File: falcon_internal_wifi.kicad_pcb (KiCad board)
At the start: 2 copper layers, 25.5 x 34.5 mm, 16 parts, among them J1 Conn_01x05, U1 LM1117-3.3, U2 ESP-12F, U3 NC7ST04M5X

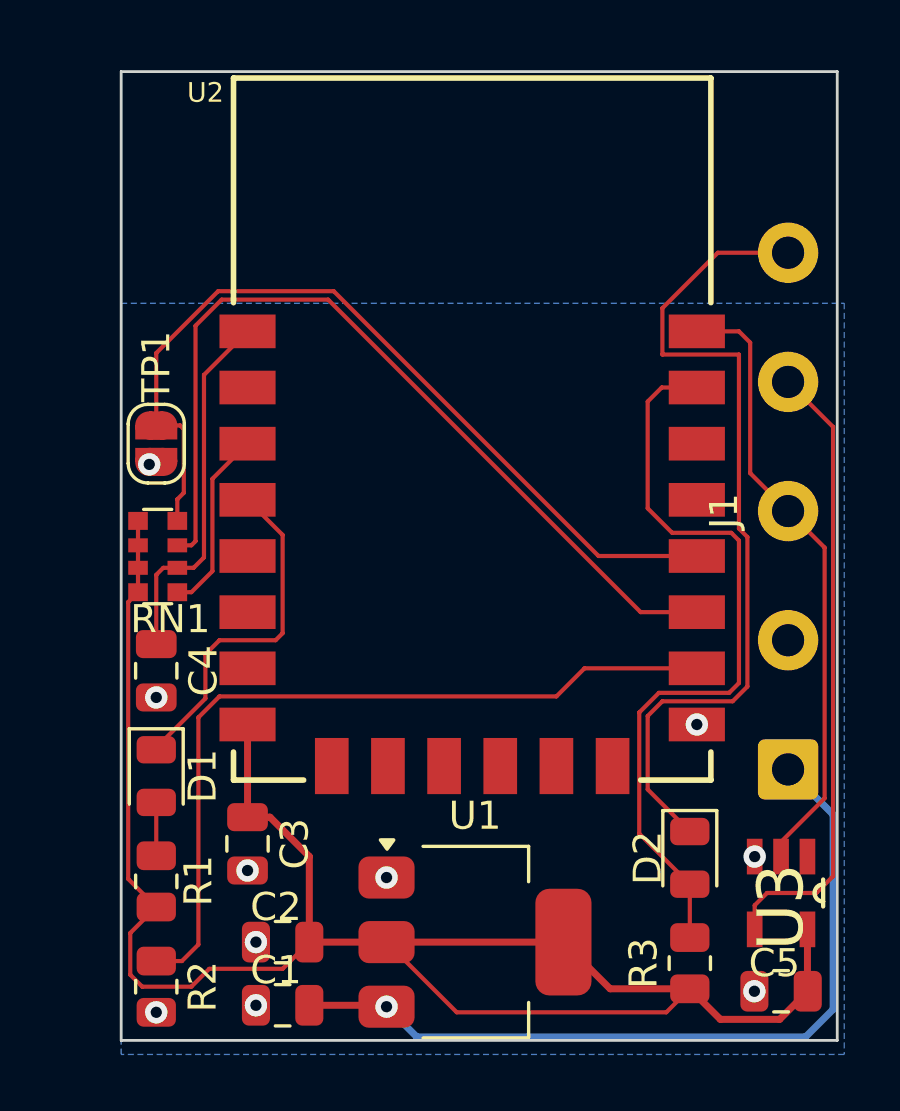
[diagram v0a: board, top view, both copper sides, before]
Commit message: Second design with smaller passive
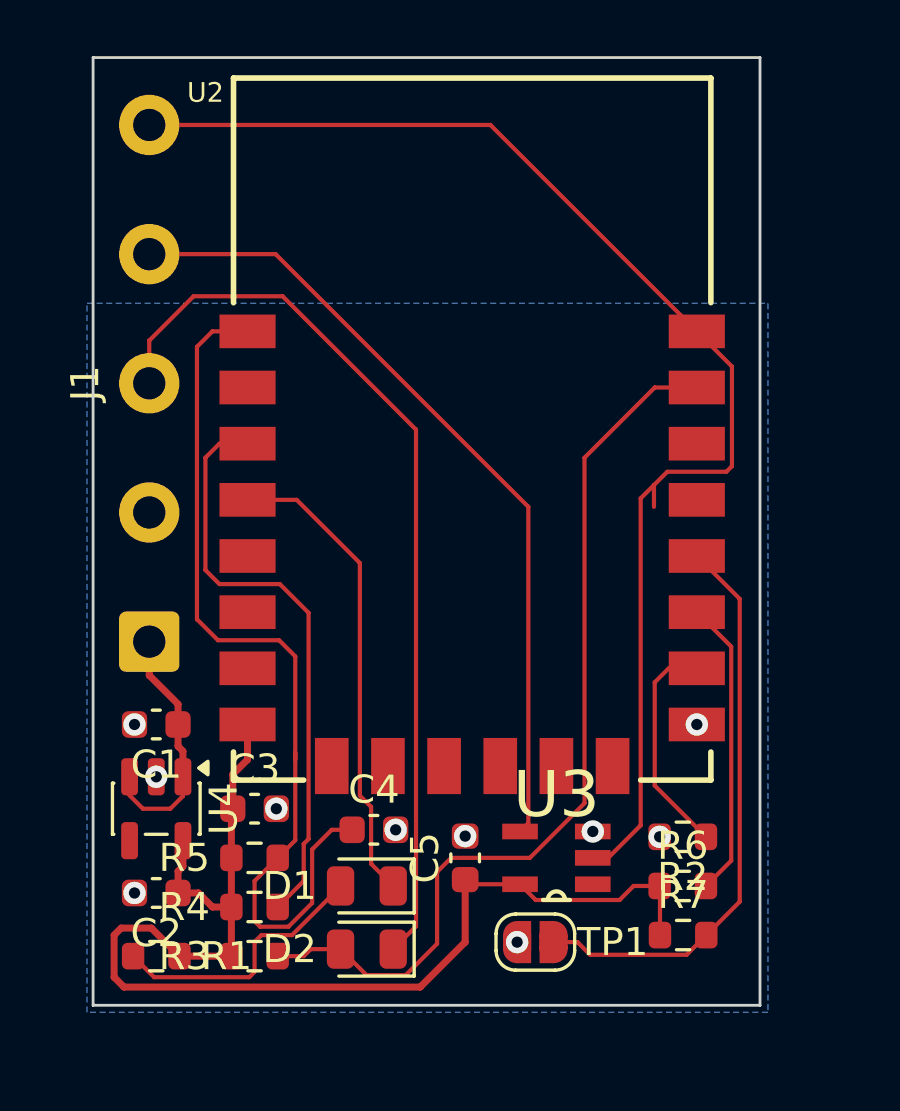
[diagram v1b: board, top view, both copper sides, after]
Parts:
- removed RN1: 10k, Resistor_SMD:R_Array_Convex_4x0612
- removed U1: LM1117-3.3, Package_TO_SOT_SMD:SOT-223-3_TabPin2
- added R4: 1k, Resistor_SMD:R_0603_1608Metric, F.Cu at (102.0, 74.5)
- added R5: 1k, Resistor_SMD:R_0603_1608Metric, F.Cu at (102.0, 72.8)
- added R6: 1k, Resistor_SMD:R_0603_1608Metric, F.Cu at (117.2, 73.8)
- added R7: 1k, Resistor_SMD:R_0603_1608Metric, F.Cu at (117.3, 75.5)
- added U4: TLV73333PDBV, Package_TO_SOT_SMD:SOT-23-5, F.Cu at (98.5, 71.0)
- C1, C2: value 1u -> 100n; footprint Capacitor_SMD:C_0805_2012Metric -> Capacitor_SMD:C_0603_1608Metric
- C3, C4, C5: footprint Capacitor_SMD:C_0805_2012Metric -> Capacitor_SMD:C_0603_1608Metric
- R1, R2, R3: footprint Resistor_SMD:R_0805_2012Metric -> Resistor_SMD:R_0603_1608Metric
- moved J1 23.2 mm to (98.2, 65.1)
- moved TP1 22.3 mm to (112.0, 75.8), turned to 180 degrees
- moved R2 19.5 mm to (117.2, 72.0), turned to 180 degrees
- moved R3 15.5 mm to (102.0, 76.2), turned to 0 degrees
- moved C5 12.2 mm to (109.5, 72.8), turned to 90 degrees
- moved D2 12.0 mm to (106.0, 76.0), turned to 180 degrees
- moved C1 11.0 mm to (98.5, 68.0)
- moved C4 9.60 mm to (106.2, 71.8), turned to 0 degrees
- moved D1 8.46 mm to (106.0, 73.8), turned to 180 degrees
- moved U3 8.10 mm to (112.8, 72.8), turned to 180 degrees
- moved C2 4.83 mm to (98.5, 74.0)
- moved R1 2.66 mm to (98.5, 76.2), turned to 180 degrees
- moved C3 1.27 mm to (102.0, 71.0), turned to 0 degrees
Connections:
- J1 pad 3: /TX -> /RX
- J1 pad 5: /RX -> /TX
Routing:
- net /TX: track 22.1 -> 46.2 mm
- net +3.3V: track 67.1 -> 43.4 mm
- net Net-(U2-GPIO2): track 31.2 -> 10.6 mm
- net Net-(U2-GPIO15): track 28.3 -> 7.96 mm
- net +5V: track 28.8 -> 8.94 mm, vias 1 -> 0
- net Net-(U2-RST): track 13.9 -> 32.2 mm
- net Net-(U2-EN): track 7.12 -> 20.9 mm
- net /FLASH: track 31.0 -> 20.5 mm
- net Net-(D1-A): track 1.90 -> 9.68 mm
- net /~{TX}: track 22.3 -> 28.9 mm
- net Net-(D2-A): track 27.3 -> 32.8 mm
- net /STATUS: track 12.5 -> 16.9 mm
- net /RX: track 30.3 -> 32.5 mm
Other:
- board size 25.5 x 34.5 mm -> 23.8 x 33.8 mm

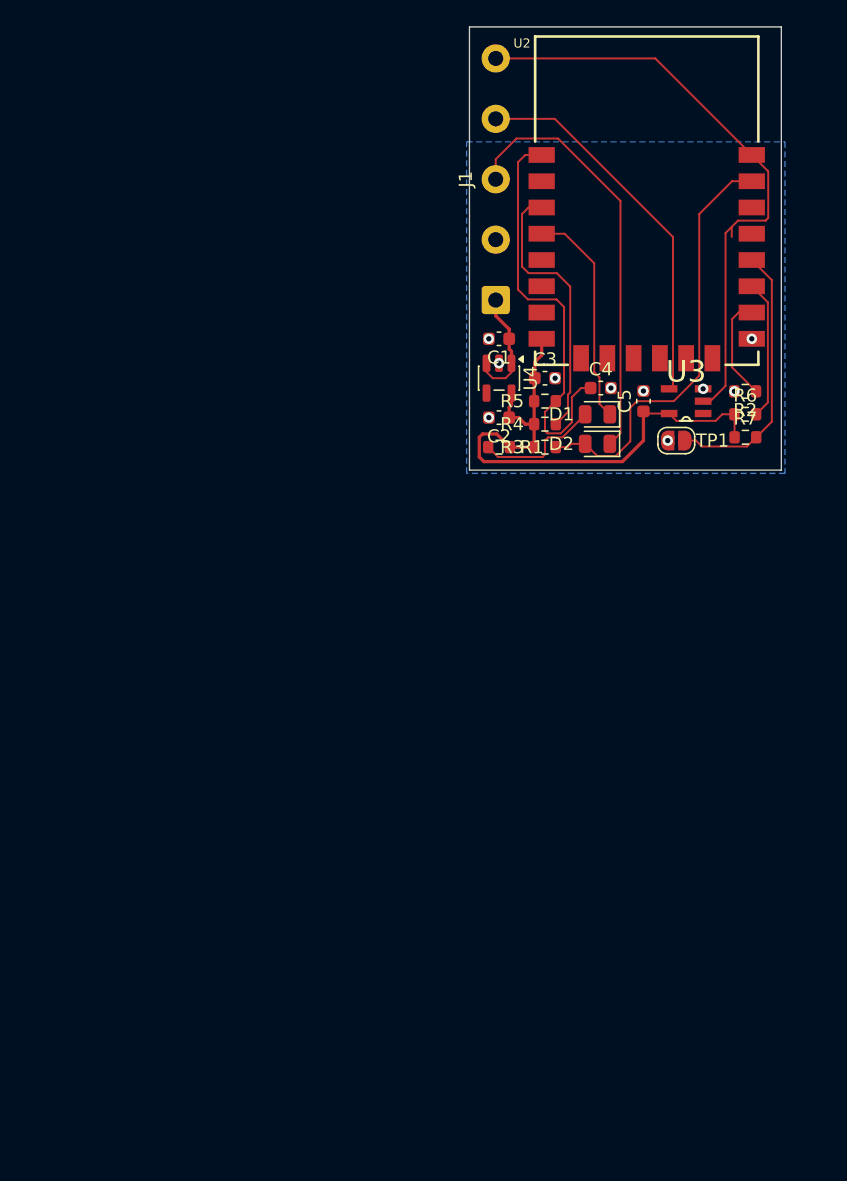
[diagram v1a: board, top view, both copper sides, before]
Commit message: Version as quoted. Considering just going back to 0805.
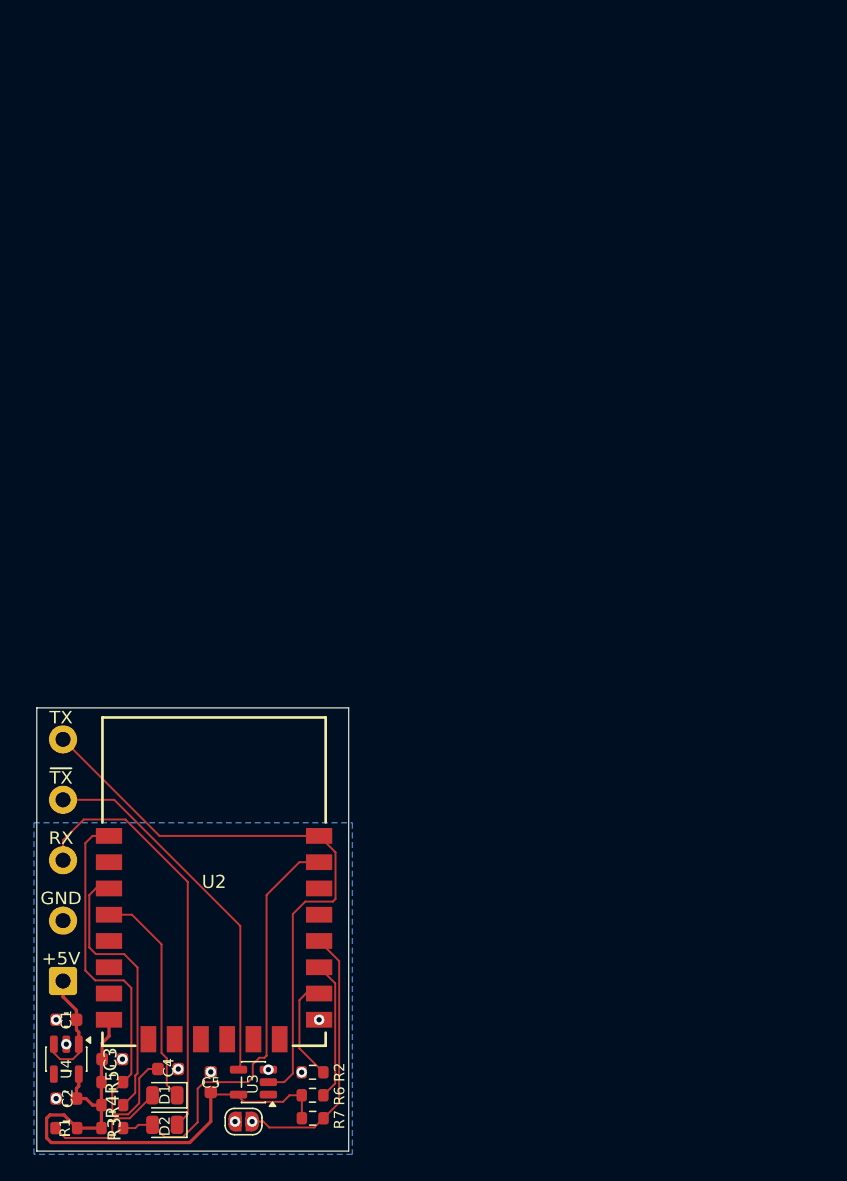
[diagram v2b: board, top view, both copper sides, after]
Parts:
- U3: footprint NC7ST04M5X:SOT95P280X145-5N -> Package_TO_SOT_SMD:SOT-23-5
- moved C1 61.4 mm to (65.5, 119.9)
- moved C2 61.4 mm to (65.5, 125.9)
- moved C3 61.4 mm to (69.0, 122.9)
- moved C4 61.4 mm to (73.3, 123.6)
- moved C5 61.4 mm to (76.5, 124.6)
- moved D1 61.4 mm to (73.0, 125.6)
- moved D2 61.4 mm to (73.0, 127.9)
- moved J1 61.4 mm to (65.3, 116.9)
- moved R2 61.4 mm to (84.3, 123.9)
- moved R4 61.4 mm to (69.0, 126.4)
- moved R5 61.4 mm to (69.0, 124.6)
- moved R6 61.4 mm to (84.3, 125.6)
- moved R7 61.4 mm to (84.3, 127.4)
- moved TP1 61.4 mm to (79.0, 127.6)
- moved U3 61.4 mm to (79.8, 124.6)
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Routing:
- net Net-(D2-A): track 32.8 -> 33.3 mm
- net /FLASH: vias 0 -> 1
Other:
- board size 23.8 x 33.8 mm -> 23.8 x 33.7 mm
- board text added: "David's Falcon Internal WIFI Board revision 1"
- board text added: "TX ~{TX} RX GND +5V"
